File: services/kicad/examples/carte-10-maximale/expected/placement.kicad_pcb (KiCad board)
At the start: 2 copper layers, 140 x 105 mm, 70 parts, among them J1 IN_5V, J10 IO0, J11 IO1, J12 IO2, J13 IO3, J14 IO4, J2 SWD, U1 STM32F103C8T6, U2 AMS1117-3.3

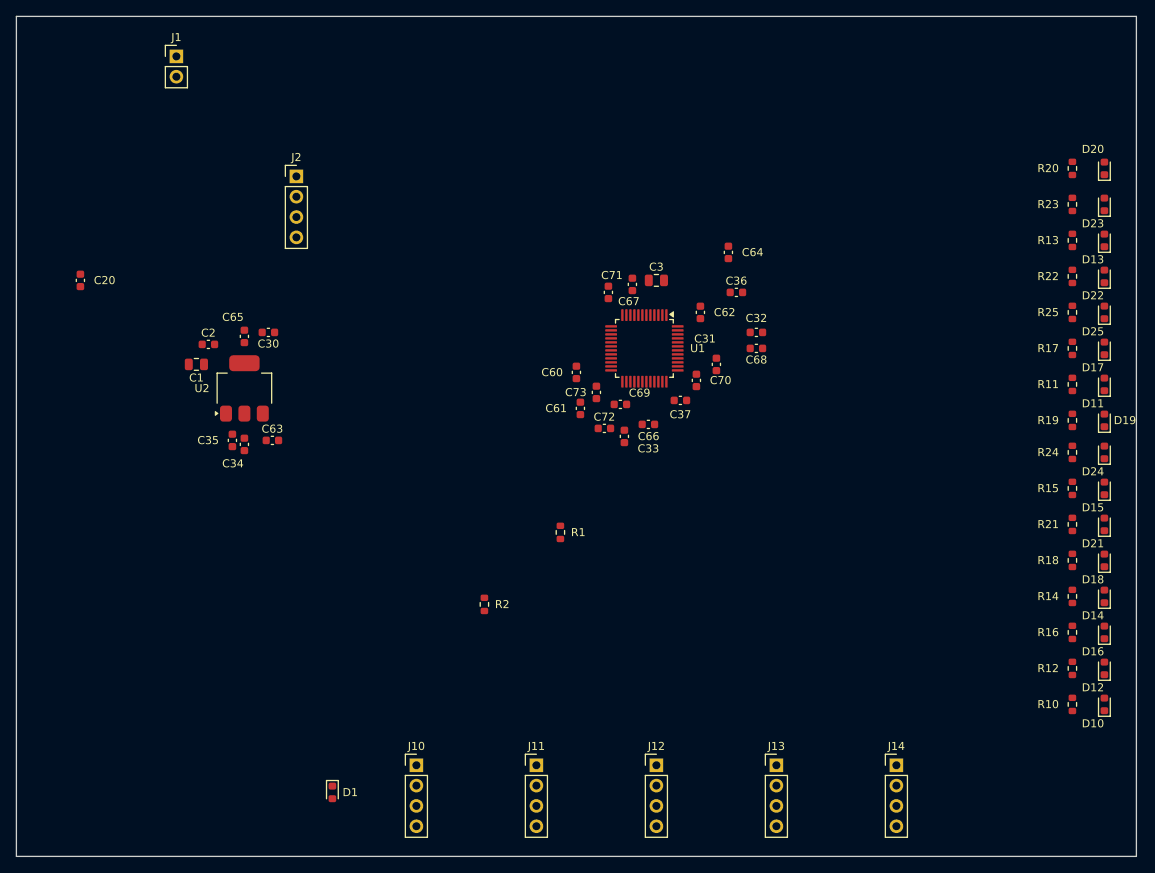
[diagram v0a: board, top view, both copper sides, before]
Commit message: chore(banc): banc en deux phases (placement valide, puis routage gele) ; relivrer carte-10 compacte (#228)
Consigne de l utilisateur : placement d abord, routage ensuite, pas
d aller-retour. Code de #226 et #227, un tirage par carte, par HTTP.

Phase A : dix placements sur dix valides — 0 erreur DRC sur le board place,
connecteur le plus loin d un bord a 2,0 mm.
Phase B : placements GELES routes. 0 erreur DRC sur les dix ; 01-05 et 10 a
0 connexion manquante ; 06:1, 07:2, 08:8, 09:11.

carte-10 relivree : 140 x 105 -> 60,9 x 45,7, 6 couches, 0 erreur,
0 manquante ; mesures.json rejuge par remesurer_banc.py, rendu refait.

08 et 09 : le board livre est celui du palier 2 couches ; les paliers 4 et 6
couches allaient plus loin (jusqu a ~96 %) puis figeaient sans rendre de
board. Tableau et journal dans BANC_DRIVER_LLM.md.


Claude-Session: https://claude.ai/code/session_01TnMqm4La2CxQHHB5K8aSSV

Co-authored-by: Claude Fable 5.1 <noreply@anthropic.com>
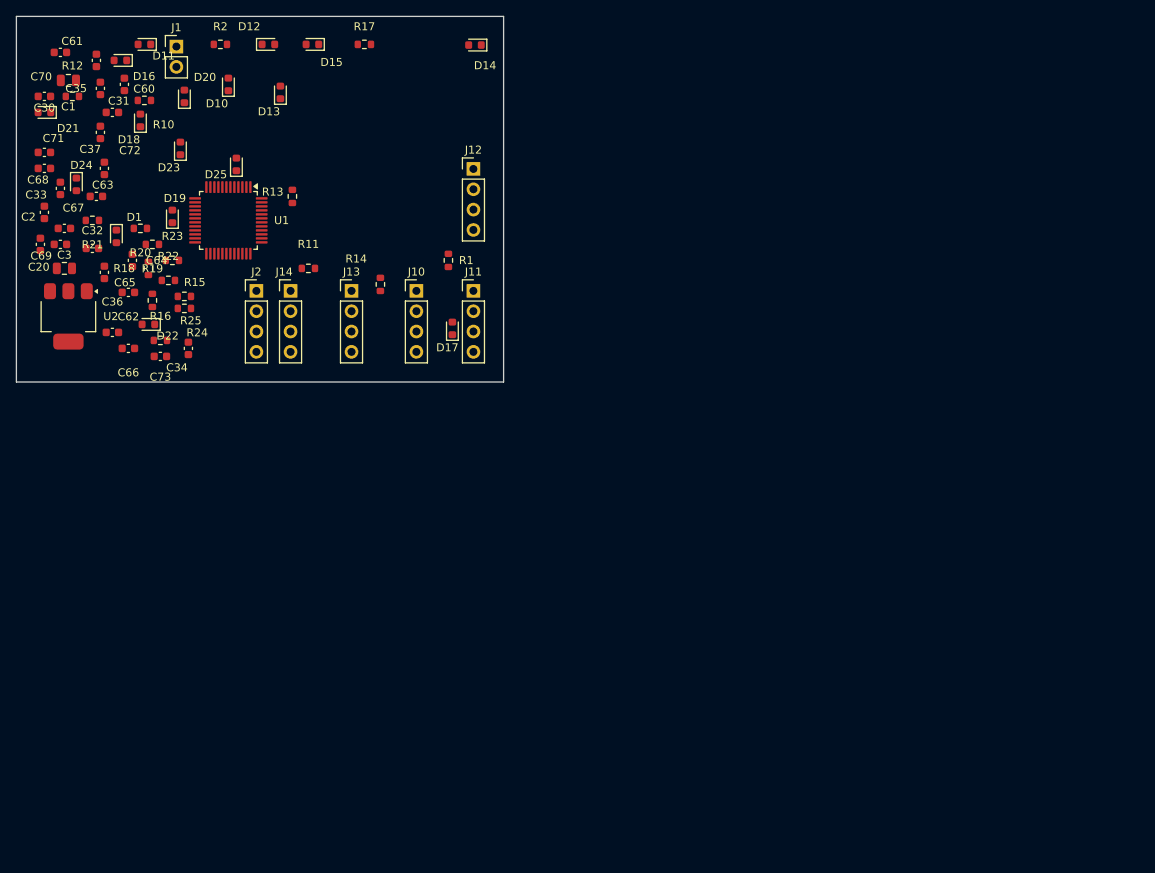
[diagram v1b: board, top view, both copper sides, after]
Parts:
- moved R12 144.0 mm to (85.5, 62.5), turned to 0 degrees
- moved D16 142.3 mm to (91.5, 58.0), turned to 180 degrees
- moved D21 142.2 mm to (82.0, 64.5), turned to 180 degrees
- moved R10 138.4 mm to (94.5, 63.0), turned to 180 degrees
- moved D10 134.2 mm to (105.0, 61.0)
- moved D24 132.8 mm to (86.0, 73.5), turned to 270 degrees
- moved D18 132.5 mm to (94.0, 65.5)
- moved D12 130.4 mm to (110.0, 56.0), turned to 0 degrees
- moved R21 128.3 mm to (88.0, 78.0), turned to 180 degrees
- moved D11 127.3 mm to (94.5, 56.0), turned to 180 degrees
- moved R18 121.1 mm to (95.0, 84.0)
- moved R16 119.7 mm to (96.5, 93.0), turned to 0 degrees
- moved D22 119.7 mm to (95.0, 91.0), turned to 180 degrees
- moved D19 119.3 mm to (98.0, 77.5)
- moved R15 117.4 mm to (95.5, 88.0), turned to 270 degrees
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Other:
- board size 140 x 105 mm -> 60.9 x 45.7 mm

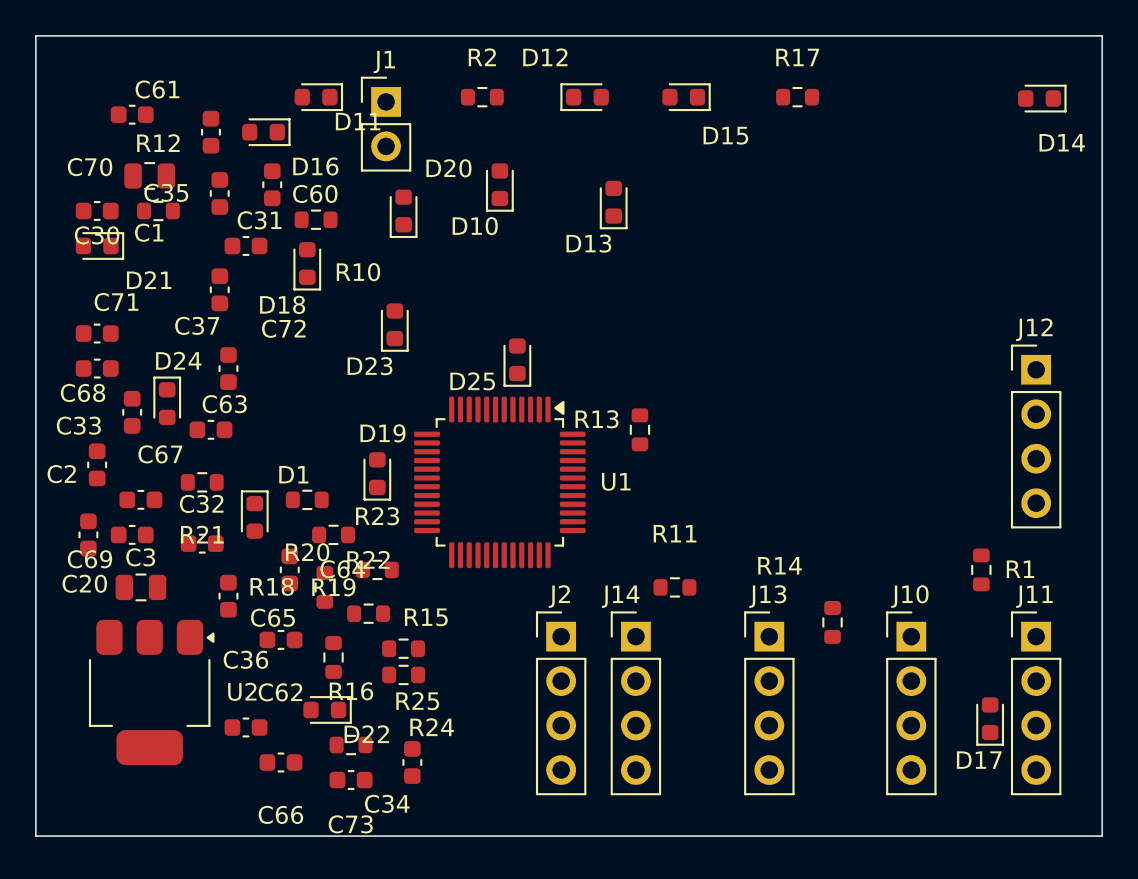
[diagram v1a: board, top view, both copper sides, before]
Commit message: feat(placement): les peripheriques se REPARTISSENT, ils ne s empilent plus
Question de l utilisateur devant le rendu : « c est quoi ce type de placement ? ».
Les composants s entassaient d un seul cote du boitier, etiquettes de
serigraphie l une sur l autre, trois quarts de la couronne vides.

TROIS CAUSES, toutes dans `_poser_les_peripheriques`, toutes la meme faute —
un angle unique pour tout un groupe :

  - les DIRECTS qui visent la meme broche (tous les decouplages d un rail,
    toutes les resistances d un meme signal) recevaient le MEME `angle_vers`
    et le meme rayon de depart ;
  - les SUIVEURS d un meme parent recevaient tous atan2(parent - centre) ;
  - les ISOLES partaient tous de l angle 0.0, c est-a-dire du meme point.

`le_long_du_rayon` ne s ecartait qu une fois la place prise : d ou la file.

REMEDE : `_ecart_en_eventail`. Le PREMIER de chaque groupe garde EXACTEMENT la
direction calculee — c est la topologie, on ne la perd pas pour faire joli — et
les suivants s ecartent symetriquement de 3 x `_PAS_ANGLE_DEG`.
Rien de deja pose ne bouge : seul l ANGLE DE DEPART de la recherche change, et
`le_long_du_rayon` reste seul juge de ce qui est libre.

BANC DES DIX CARTES, contour resserre ET peripheriques repartis :

    carte             demandee    livree         err  manq
    carte-01           25 x 20    20,1 x 13,6     0    0
    carte-02           55 x 40    34,9 x 25,2     0    0
    carte-03           50 x 35    27,6 x 19,9     0    0
    carte-04           60 x 45    36,6 x 29,8     0    0
    carte-05           70 x 50    40,0 x 32,6     0    0
    carte-06           80 x 60    46,5 x 36,4     0    0
    carte-07          110 x 80    47,7 x 38,8     0    0
    carte-08          125 x 95    57,4 x 44,1     0    0
    carte-09          130 x 100   57,8 x 45,2     0    0
    carte-10          140 x 105   59,0 x 45,8     0    0

Dix sur dix, 100 % route. carte-07 gagne 5,5 mm de largeur sur le passage
precedent, carte-06 deux, carte-10 deux. Sur ca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
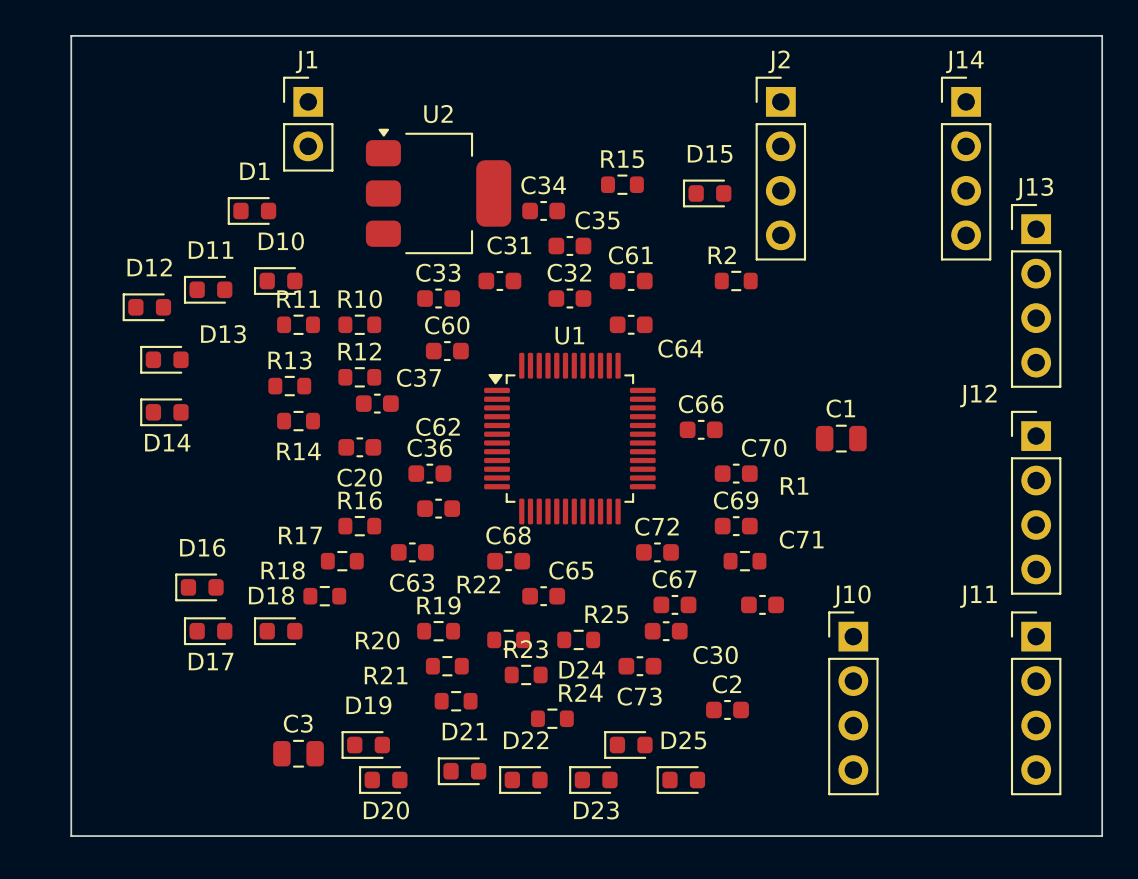
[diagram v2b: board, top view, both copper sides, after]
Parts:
- moved D14 52.9 mm to (86.0, 74.0), turned to 0 degrees
- moved D17 44.8 mm to (88.5, 86.5), turned to 0 degrees
- moved C1 42.3 mm to (124.5, 75.5), turned to 0 degrees
- moved C71 41.0 mm to (120.0, 85.0)
- moved C30 40.4 mm to (114.5, 86.5), turned to 0 degrees
- moved C70 40.1 mm to (118.5, 77.5), turned to 0 degrees
- moved C2 38.6 mm to (118.0, 91.0), turned to 0 degrees
- moved R17 37.1 mm to (96.0, 82.5)
- moved D21 36.6 mm to (103.0, 94.5), turned to 0 degrees
- moved J14 35.9 mm to (131.6, 56.3)
- moved C69 34.5 mm to (118.5, 80.5), turned to 0 degrees
- moved J2 33.0 mm to (121.0, 56.3)
- moved U2 32.9 mm to (101.5, 61.5), turned to 0 degrees
- moved D24 32.9 mm to (112.5, 93.0), turned to 0 degrees
- moved R14 32.6 mm to (93.5, 74.5), turned to 0 degrees
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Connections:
- C3 pad 1: +3V3 -> Net-(C3-1)
- U1 pad 36: +3V3 -> PWR_FLAG
- U1 pad 48: +3V3 -> PWR_FLAG
- U1 pad 9: IO_L5 -> PWR_FLAG
- U2 pad 2: +3V3 -> Net-(U2-2)
- U2 pad 3: VIN -> PWR_FLAG
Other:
- board size 60.9 x 45.7 mm -> 58.9 x 45.7 mm
